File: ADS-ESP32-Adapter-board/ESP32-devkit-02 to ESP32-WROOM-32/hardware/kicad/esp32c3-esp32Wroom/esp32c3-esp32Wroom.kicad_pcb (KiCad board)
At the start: 2 copper layers, 4 parts, among them J1 Conn_01x15_esp32_devkit_V1_el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, J2 Conn_01x15_esp32_devkit_V1_el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, J3 Conn_01x15_esp32_c3_devkit_02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, J4 Conn_01x15_esp32_c3_devkit_02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

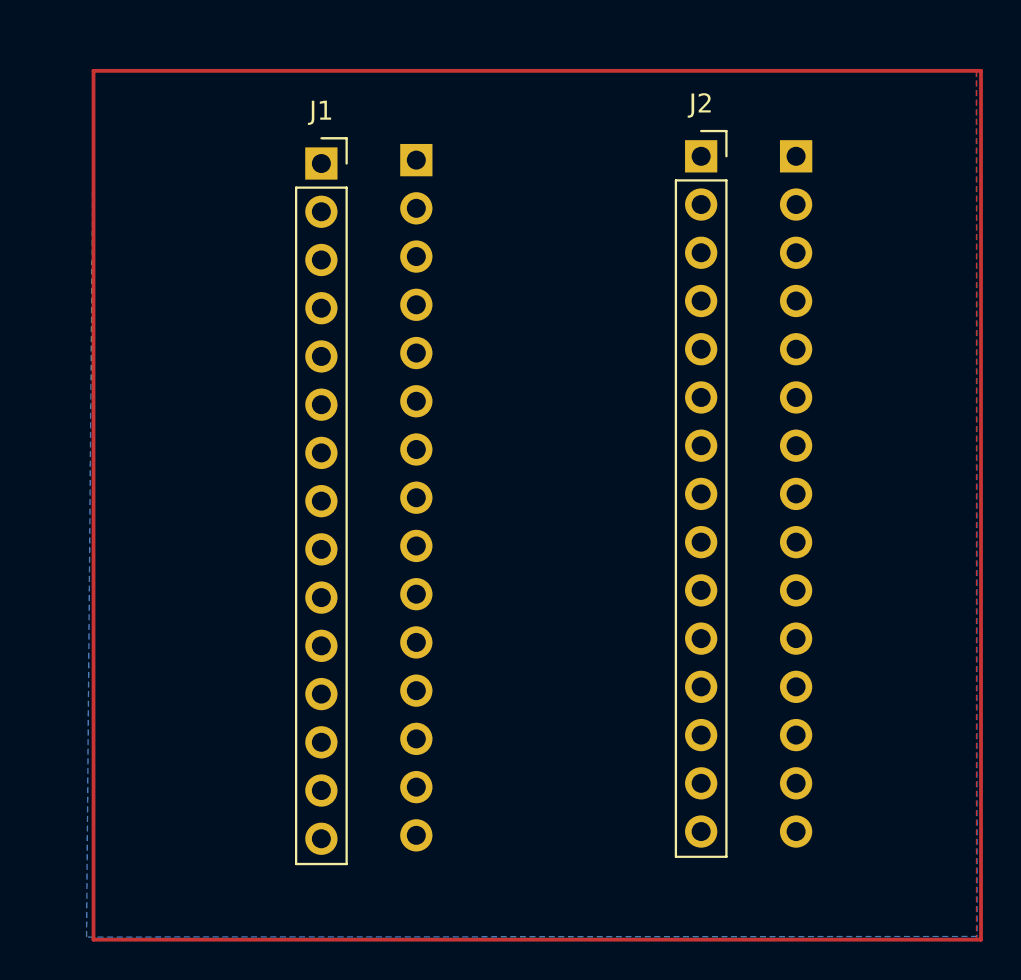
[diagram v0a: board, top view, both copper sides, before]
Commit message: Esquema terminado, PCB terminada pero falta agregar algún símbolo que indique la posición, asegurar que las ancho pistas es adecuado y que no haya acoplamiento entre pistas.
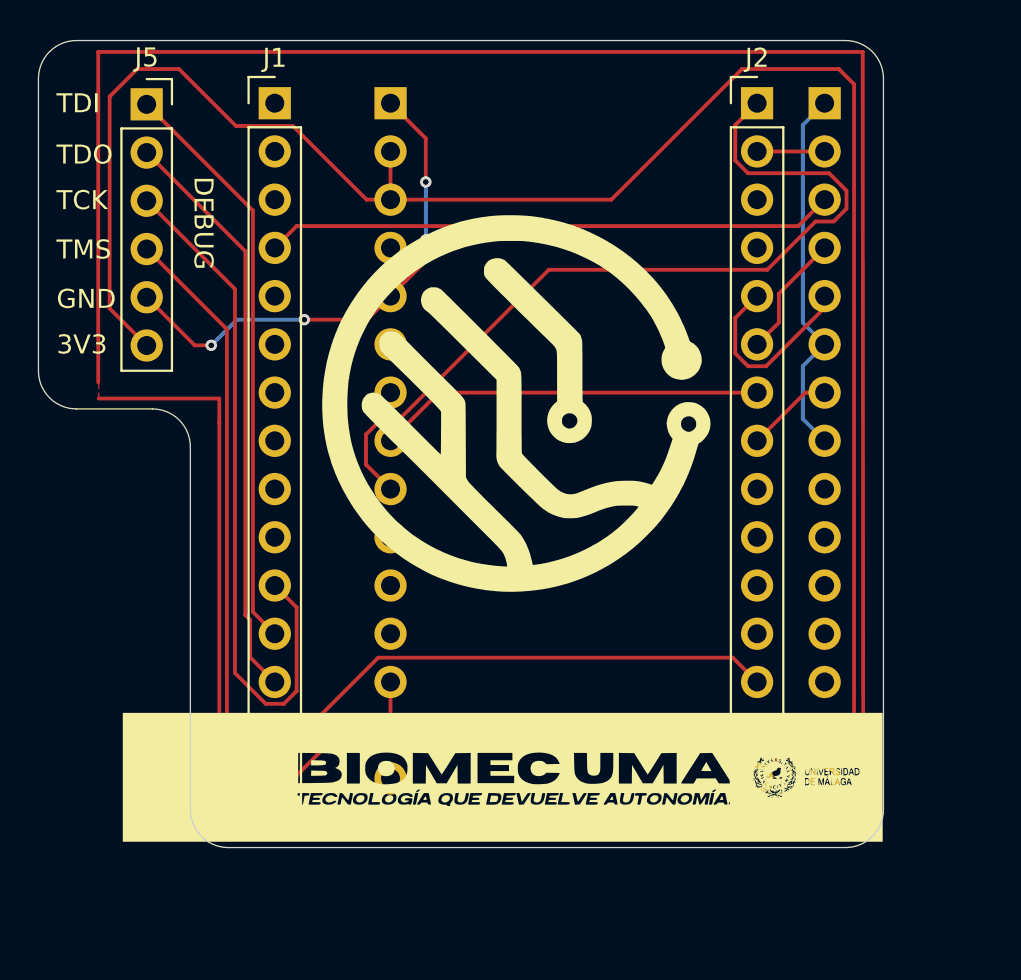
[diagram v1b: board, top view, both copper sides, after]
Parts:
- added G***: LOGO, kicad:logo25x25, F.Cu at (132.8, 74.0)
- added G***: LOGO, kicad:biomecumabanner, F.Cu at (132.1, 93.7)
- added G***: LOGO, kicad:banner recortado, B.Cu at (135.7, 76.2)
- added J5: Conn_01x06, Connector_PinSocket_2.54mm:PinSocket_1x06_P2.54mm_Vertical, F.Cu at (113.3, 58.3)
- J1, J2: footprint Connector_PinSocket_2.54mm:PinSocket_1x15_P2.54mm_Vertical -> Connector_PinHeader_2.54mm:PinHeader_1x15_P2.54mm_Vertical
- moved J2 4.06 mm to (145.4, 58.2)
- moved J1 4.01 mm to (120.0, 58.2)
- moved J3 3.29 mm to (126.1, 58.2)
- moved J4 3.17 mm to (149.0, 58.2)
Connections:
- J1 pad 1: (no net) -> unconnected-(J1-EN-Pad1)
- J1 pad 10: (no net) -> unconnected-(J1-D27-Pad10)
- J1 pad 11: (no net) -> /TCK
- J1 pad 12: (no net) -> /TDI
- J1 pad 13: (no net) -> /TDO
- J1 pad 14: (no net) -> /GND
- J1 pad 15: (no net) -> /5V
- J1 pad 2: (no net) -> unconnected-(J1-VP-Pad2)
- J1 pad 3: (no net) -> unconnected-(J1-VN-Pad3)
- J1 pad 4: (no net) -> /FE_DRDY
- J1 pad 5: (no net) -> unconnected-(J1-D35-Pad5)
- J1 pad 6: (no net) -> unconnected-(J1-D32-Pad6)
- J1 pad 7: (no net) -> unconnected-(J1-D33-Pad7)
- J1 pad 8: (no net) -> unconnected-(J1-D25-Pad8)
- J1 pad 9: (no net) -> unconnected-(J1-D26-Pad9)
- J2 pad 1: (no net) -> /SPI1_MOSI
- J2 pad 10: (no net) -> unconnected-(J2-RX2-Pad10)
- J2 pad 11: (no net) -> unconnected-(J2-D4-Pad11)
- J2 pad 12: (no net) -> unconnected-(J2-D2-Pad12)
- J2 pad 13: (no net) -> /TMS
- J2 pad 14: (no net) -> /GND
- J2 pad 15: (no net) -> /3V3
- J2 pad 2: (no net) -> /FE_RESET
- J2 pad 3: (no net) -> unconnected-(J2-TX0-Pad3)
- J2 pad 4: (no net) -> unconnected-(J2-RX0-Pad4)
- J2 pad 5: (no net) -> /FE_START
- J2 pad 6: (no net) -> /SPI1_MISO
- J2 pad 7: (no net) -> /SPI1_SCLK
- J2 pad 8: (no net) -> /FE_CS
- J2 pad 9: (no net) -> unconnected-(J2-TX2-Pad9)
- J3 pad 1: (no net) -> /GND
- J3 pad 10: (no net) -> /GND
- J3 pad 11: (no net) -> unconnected-(J3-8-Pad11)
- J3 pad 12: (no net) -> unconnected-(J3-9-Pad12)
- J3 pad 13: (no net) -> /5V
- J3 pad 14: (no net) -> /5V
- J3 pad 15: (no net) -> /GND
- J3 pad 2: (no net) -> /3V3
- J3 pad 3: (no net) -> /3V3
- J3 pad 5: unconnected-(J3-Pin_7-Pad5) -> /GND
- J3 pad 6: SPI1_SCLK -> unconnected-(J3-4-Pad6)
- J3 pad 7: SPI1_MOSI -> unconnected-(J3-5-Pad7)
- J3 pad 8: unconnected-(J3-Pin_11-Pad8) -> /SPI1_SCLK
- J3 pad 9: unconnected-(J3-Pin_12-Pad9) -> /SPI1_MOSI
- J4 pad 1: FE_DRDY -> /GND
- J4 pad 10: FE_CS -> unconnected-(J4-TX-Pad10)
- J4 pad 11: (no net) -> /GND
- J4 pad 12: (no net) -> unconnected-(J4-18-Pad12)
- J4 pad 13: (no net) -> unconnected-(J4-19-Pad13)
- J4 pad 14: (no net) -> /GND
- J4 pad 15: (no net) -> /GND
- J4 pad 2: SPI1_MISO -> /FE_RESET
- J4 pad 3: FE_START -> /FE_DRDY
- J4 pad 4: (no net) -> /SPI1_MISO
- J4 pad 5: (no net) -> /FE_START
- J4 pad 6: (no net) -> /GND
- J4 pad 7: (no net) -> /FE_CS
- J4 pad 8: (no net) -> /GND
- J4 pad 9: (no net) -> unconnected-(J4-RX-Pad9)
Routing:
- net /3V3: track 0.00 -> 102.7 mm
- net /TMS: track 0.00 -> 57.6 mm
- net /GND: track 0.00 -> 46.5 mm, vias 0 -> 4
- net /SPI1_MOSI: track 0.00 -> 44.6 mm
- net /TCK: track 0.00 -> 37.0 mm
- net /TDO: track 0.00 -> 30.7 mm
- net /TDI: track 0.00 -> 30.7 mm
- net /FE_DRDY: track 0.00 -> 30.0 mm
- net /SPI1_SCLK: track 0.00 -> 20.4 mm
- net /FE_START: track 0.00 -> 10.4 mm
- net /5V: track 0.00 -> 9.69 mm
- net /SPI1_MISO: track 0.00 -> 6.55 mm
- net /FE_CS: track 0.00 -> 4.61 mm
- net /FE_RESET: track 0.00 -> 3.56 mm
- added copper zone on F.Cu, net /GND
- removed copper zone on B.Cu, net (none)
- removed copper zone on F.Cu, net (none)
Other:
- board outline added: 44.5 x 42.5 mm
- board text added: "3V3"
- board text added: "DEBUG"
- board text added: "GND"
- board text added: "TCK"
- board text added: "TDI"
- board text added: "TDO"
- board text added: "TMS"

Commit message: Refactor code structure for improved readability and maintainability
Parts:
- moved G*** 0.70 mm to (132.1, 94.4)
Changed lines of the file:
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@@
 		(capping no)
 		(filling no)
-		(zone_defaults)
 		(grid_origin 115.6 97.403444)
 		(pcbplotparams
@@
 	(footprint "kicad:biomecumabanner"
 		(layer "F.Cu")
-		(at 132.05 93.703444)
+		(at 132.05 94.403444)
 		(property "Reference" "G***"
 			(at 0 0 0)

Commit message: Refactor code structure for improved readability and maintainability
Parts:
- J1, J2: footprint Connector_PinHeader_2.54mm:PinHeader_1x15_P2.54mm_Vertical -> Connector_PinSocket_2.54mm:PinSocket_1x15_P2.54mm_Vertical
- moved G*** 0.60 mm to (132.8, 73.4)
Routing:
- net /GND: track 46.5 -> 45.4 mm
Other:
- board text added: "Adapter board for ADS1198 board by Biomec"
- board text added: "D12"
- board text added: "D13"
- board text added: "D14"
- board text added: "D15"
- board text added: "D2"
- board text added: "D22"
- board text added: "D23"
- board text added: "D27"
- board text added: "D34"
- board text added: "D4"
- board text added: "EN"
- board text added: "ESP32-DEVKIT-02 TO ESP32-DEVKIT-V1"
- board text added: "ESP32-DEVKIT-V1"
- board text added: "RX0"
- board text added: "RX2"
- board text added: "TX0"
- board text added: "VN"
- board text added: "VP"

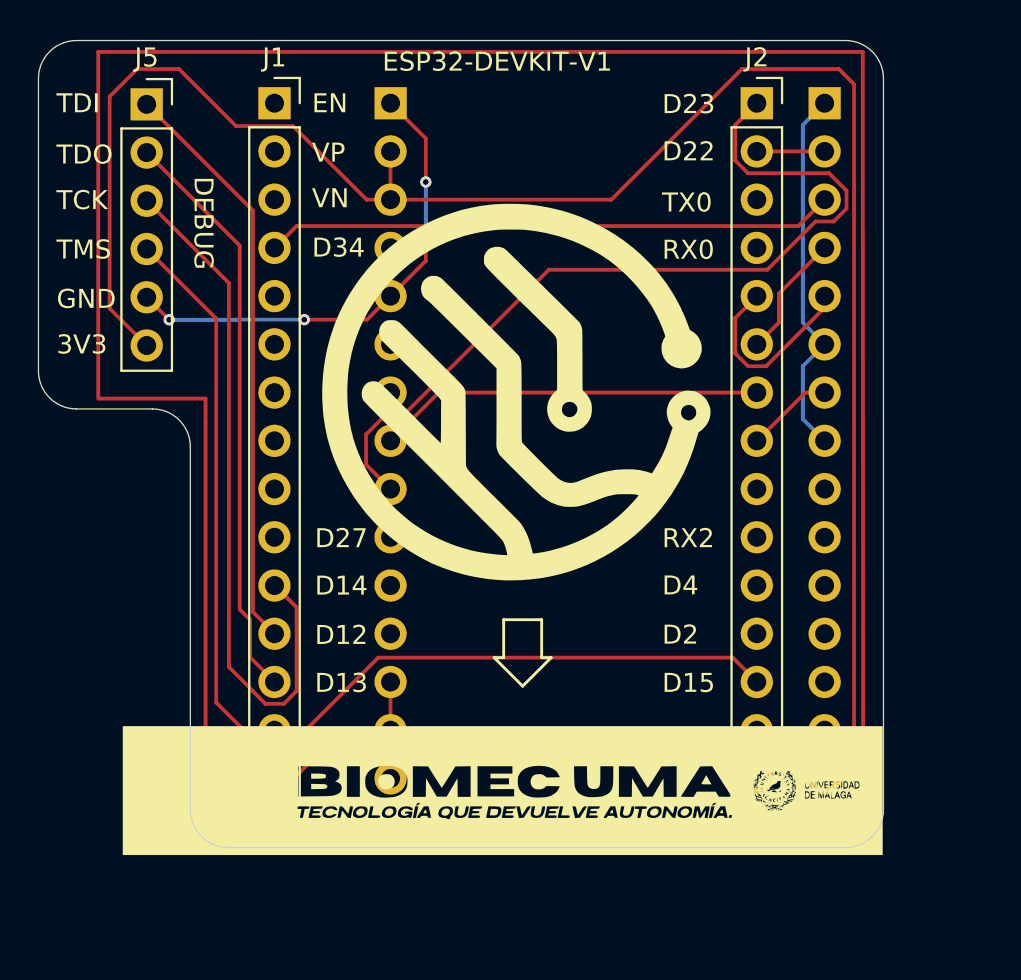
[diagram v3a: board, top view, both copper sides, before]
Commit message: Add additional text annotations to schematic and update visible layers in PCB layout
- Added JTAG, GND, GPIO, Source, and SPI text annotations to the schematic for better clarity and reference.
- Updated the visible layers in the PCB layout file to include grid visibility.
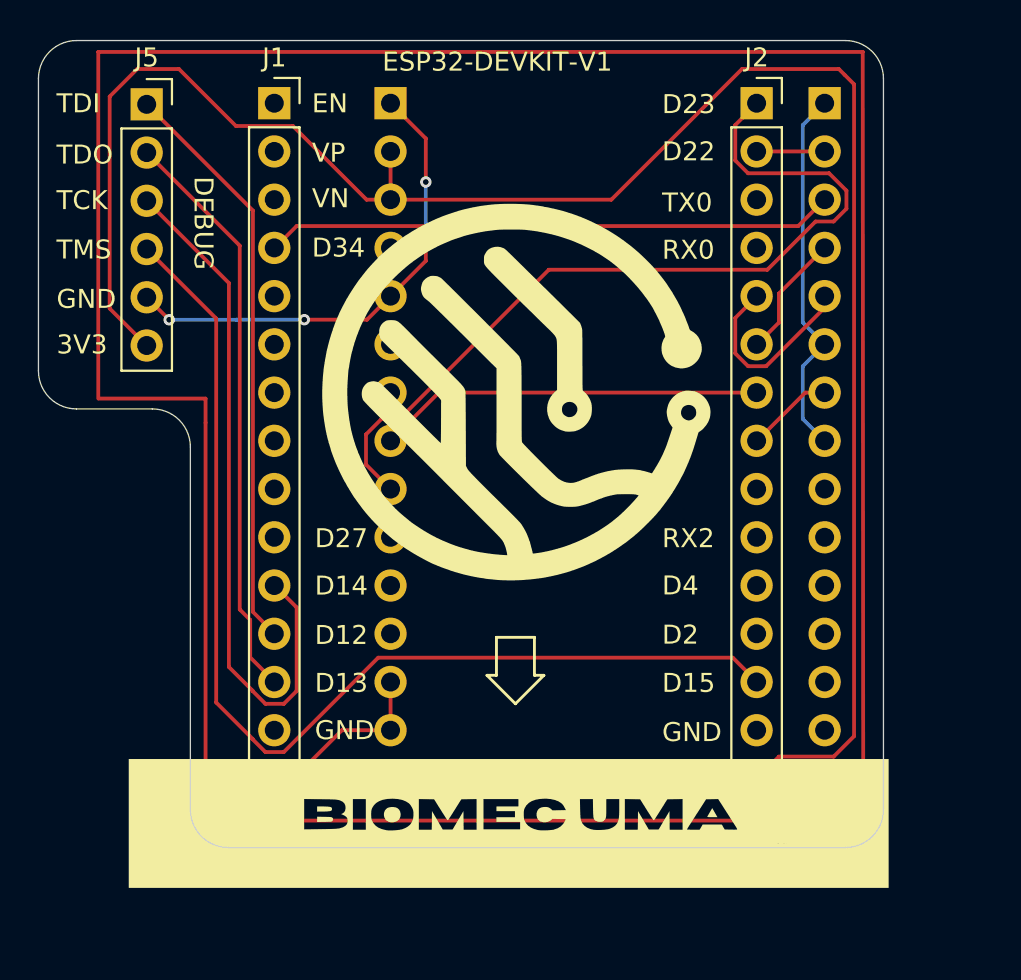
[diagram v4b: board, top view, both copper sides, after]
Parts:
- moved G*** 1.76 mm to (132.4, 96.1)
